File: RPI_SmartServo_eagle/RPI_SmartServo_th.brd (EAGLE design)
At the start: 75 x 60 mm, 39 parts, among them Q1 MCP9701A-E/TO, U1 ZXCT1009

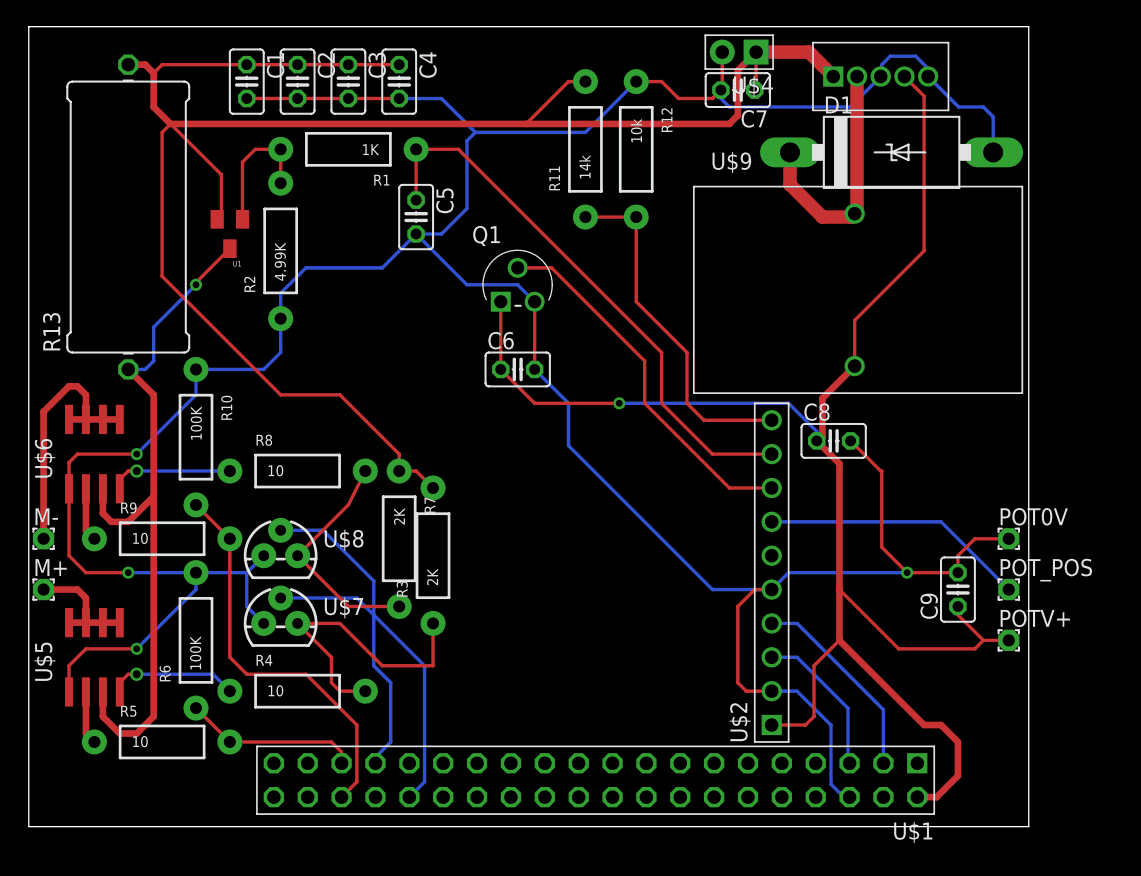
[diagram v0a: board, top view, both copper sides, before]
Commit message: Ground plane added 	modificado: RPI_SmartServo_eagle/RPI_SmartServo_th.brd
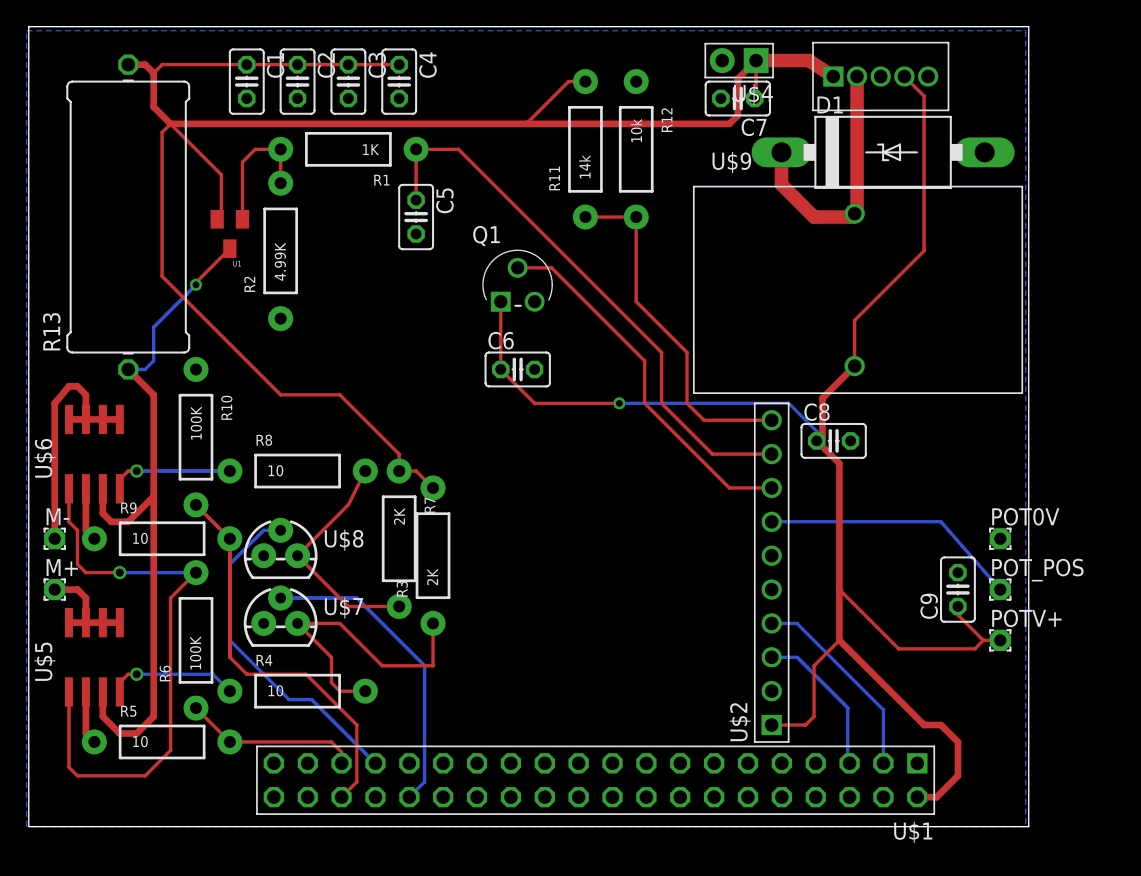
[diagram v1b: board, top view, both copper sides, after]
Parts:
- moved M+ 0.83 mm to (2.10, 17.8)
- moved M- 0.83 mm to (2.10, 21.6)
- moved D1 0.64 mm to (64.2, 50.6)
- moved C7 0.63 mm to (53.3, 54.6)
- moved U$4 0.63 mm to (54.7, 57.5)
- moved POT0V 0.63 mm to (73.0, 21.6)
- moved POTV+ 0.63 mm to (73.0, 14.0)
- moved POT_POS 0.63 mm to (73.0, 17.8)
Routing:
- net GND: track 257.3 -> 43.5 mm, vias 4 -> 1
- net EN_A: track 30.0 -> 42.5 mm
- net PWM_1: track 23.2 -> 25.3 mm
- net +12V: track 136.7 -> 135.7 mm
- net N$4: track 9.09 -> 8.26 mm
- net +5V: track 124.8 -> 124.2 mm
- net N$10: track 18.7 -> 19.4 mm
- added copper zone on layer 16, net GND

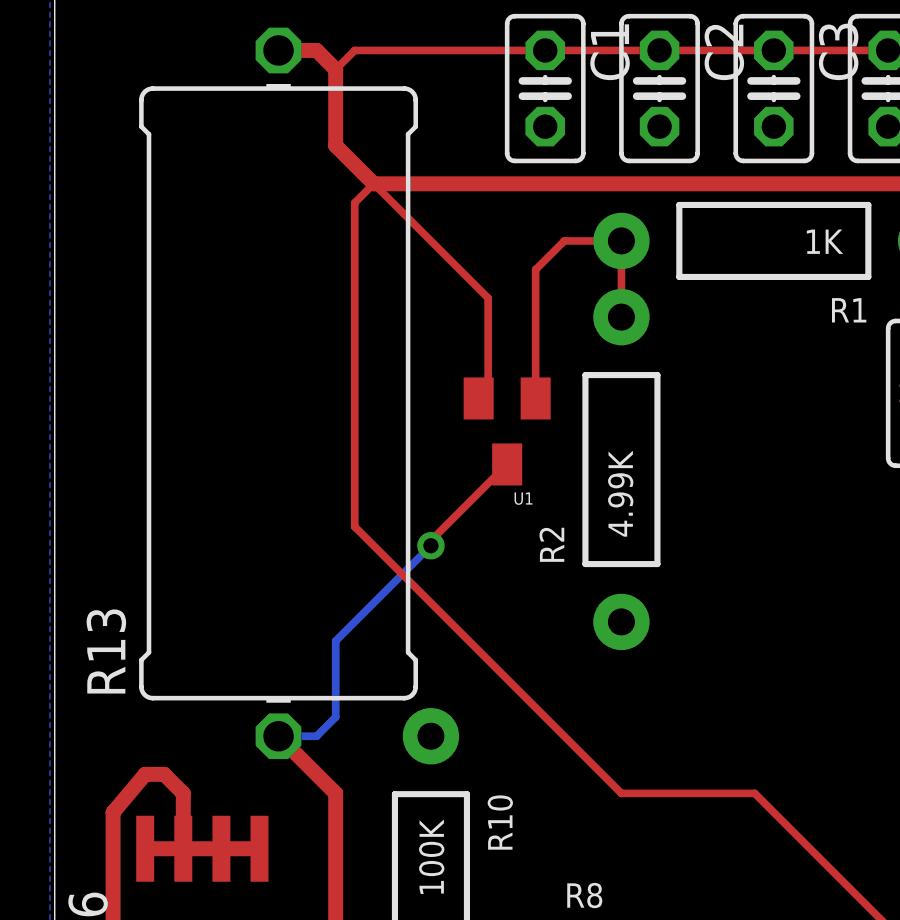
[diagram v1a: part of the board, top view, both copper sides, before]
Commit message: Changed the Current Sensor 	modificado: RPI_SmartServo_eagle/RPI_SmartServo_th.brd 	modificado: RPI_SmartServo_eagle/RPI_SmartServo_th.sch
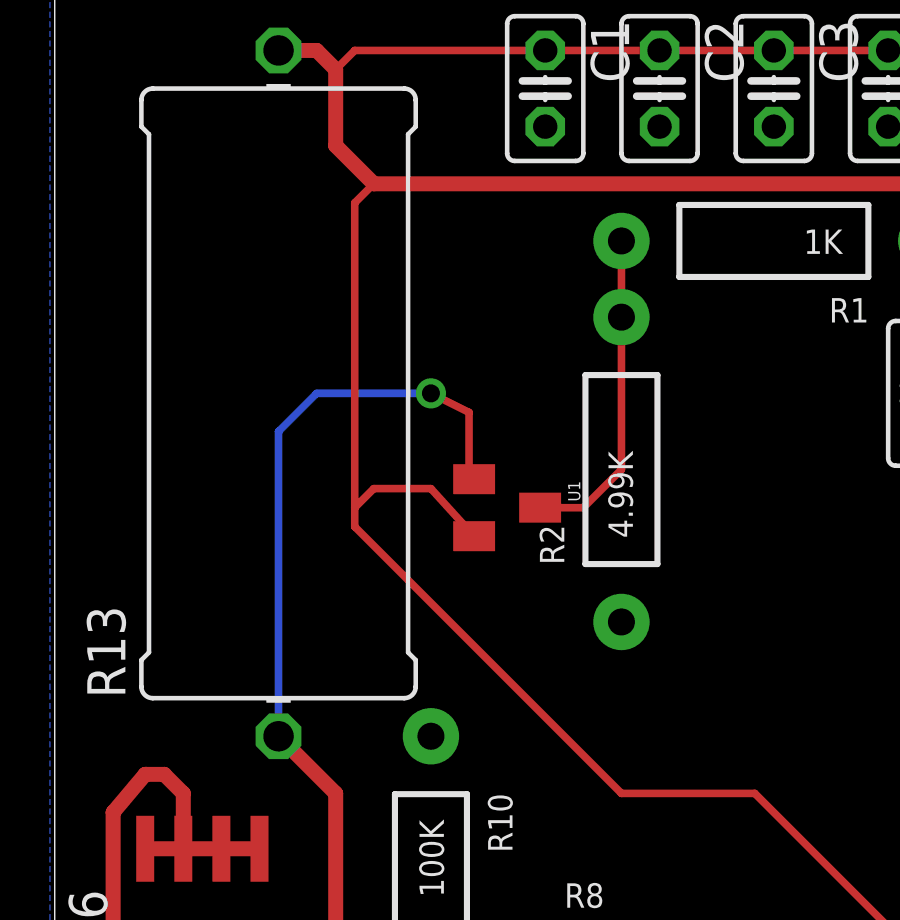
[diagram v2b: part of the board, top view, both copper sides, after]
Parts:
- U1: device WSNlib:SOT23 -> 00LibreriaErle:SOT23
- moved U1 2.54 mm to (15.2, 41.9), turned to 270 degrees
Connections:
- net N$1: now also U1.3; no longer U1.1
- net N$12: now also U1.1; no longer U1.3
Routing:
- net N$12: track 53.2 -> 59.7 mm
- net +12V: track 135.7 -> 131.7 mm
- net N$1: track 10.1 -> 10.9 mm
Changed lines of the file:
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@@
 <wire x1="75.16" y1="60" x2="0.16" y2="60" width="0" layer="20"/>
 <wire x1="0.16" y1="60" x2="0.16" y2="0" width="0" layer="20"/>
+<dimension x1="0" y1="0" x2="0.16" y2="60" x3="-10.239096875" y3="30.027515625" textsize="1.778" layer="1"/>
+<dimension x1="0" y1="0" x2="75.16" y2="0" x3="37.58" y3="-12.7" textsize="1.778" layer="1"/>
+<dimension x1="75" y1="0" x2="10" y2="0" x3="42.5" y3="-5.715" textsize="1.778" layer="1"/>
+<dimension x1="0" y1="0" x2="0" y2="30" x3="-5.08" y3="15" textsize="1.778" layer="1"/>
 </plain>
 <attributes>
@@
 <element name="U$8" library="00LibreriaErle" package="TO-92" value="2N7008G" x="19.05" y="20.32"/>
 <element name="U$9" library="00LibreriaErle" package="KM-4" value="PE-53113NL" x="50.038" y="48.006"/>
-<element name="U1" library="WSNlib" package="SOT23" value="ZXCT1009" x="15.24" y="44.45" rot="R180"/>
 <element name="Q1" library="00LibreriaErle" package="TO127P254X533-3" value="MCP9701A-E/TO" x="38.1" y="41.91">
 <attribute name="SUPPLIER" value="Microchip" x="38.1" y="41.91" size="1.778" layer="27" display="off"/>
@@
 <element name="M+" library="wirepad" package="1,6/0,9" value="" x="2.105" y="17.78"/>
 <element name="M-" library="wirepad" package="1,6/0,9" value="" x="2.105" y="21.59"/>
+<element name="U1" library="00LibreriaErle" package="SOT23" value="ZXCT1009" x="15.24" y="41.91" rot="R270"/>
 </elements>
 <signals>
@@
 <signal name="N$1">
 <contactref element="R1" pad="P$2"/>
-<contactref element="U1" pad="1"/>
 <contactref element="R2" pad="P$2"/>
 <wire x1="19.05" y1="48.26" x2="19.05" y2="50.8" width="0.254" layer="1"/>
-<wire x1="19.05" y1="50.8" x2="17.145" y2="50.8" width="0.254" layer="1"/>
-<wire x1="17.145" y1="50.8" x2="16.19" y2="49.845" width="0.254" layer="1"/>
-<wire x1="16.19" y1="49.845" x2="16.19" y2="45.55" width="0.254" layer="1"/>
+<contactref element="U1" pad="3"/>
+<wire x1="16.34" y1="41.91" x2="17.78" y2="41.91" width="0.254" layer="1"/>
+<wire x1="17.78" y1="41.91" x2="19.05" y2="43.18" width="0.254" layer="1"/>
+<wire x1="19.05" y1="43.18" x2="19.05" y2="48.26" width="0.254" layer="1"/>
 </signal>
 <signal name="CURRENT">
@@
 </signal>
 <signal name="N$12">
-<contactref element="U1" pad="3"/>
 <contactref element="R13" pad="1"/>
 <contactref element="U$5" pad="3"/>
@@
 <wire x1="9.525" y1="8.255" x2="9.525" y2="24.765" width="0.5" layer="1"/>
 <wire x1="5.715" y1="23.495" x2="5.715" y2="25.34" width="0.5" layer="1"/>
-<wire x1="15.24" y1="43.35" x2="12.7" y2="40.81" width="0.254" layer="1"/>
-<wire x1="12.7" y1="40.81" x2="12.7" y2="40.64" width="0.254" layer="1"/>
-<via x="12.7" y="40.64" extent="1-16" drill="0.508" shape="square"/>
-<wire x1="12.7" y1="40.64" x2="9.525" y2="37.465" width="0.254" layer="16"/>
-<wire x1="9.525" y1="37.465" x2="9.525" y2="34.925" width="0.254" layer="16"/>
-<wire x1="9.525" y1="34.925" x2="8.89" y2="34.29" width="0.254" layer="16"/>
-<wire x1="8.89" y1="34.29" x2="7.62" y2="34.29" width="0.254" layer="16"/>
+<contactref element="U1" pad="1"/>
+<wire x1="7.62" y1="34.29" x2="7.62" y2="44.45" width="0.254" layer="16"/>
+<wire x1="7.62" y1="44.45" x2="8.89" y2="45.72" width="0.254" layer="16"/>
+<wire x1="8.89" y1="45.72" x2="12.7" y2="45.72" width="0.254" layer="16"/>
+<via x="12.7" y="45.72" extent="1-16" drill="0.6" shape="square"/>
+<wire x1="12.7" y1="45.72" x2="13.97" y2="45.085" width="0.254" layer="1"/>
+<wire x1="13.97" y1="45.085" x2="13.97" y2="43.18" width="0.254" layer="1"/>
+<wire x1="13.97" y1="43.18" x2="14.14" y2="42.86" width="0.254" layer="1"/>
 </signal>
 <signal name="N$10">
@@
 <contactref element="U$3" pad="1"/>
 <contactref element="C7" pad="1"/>
-<contactref element="U1" pad="2"/>
 <contactref element="R13" pad="2"/>
 <contactref element="C4" pad="1"/>
@@
 <wire x1="24.13" y1="57.15" x2="27.94" y2="57.15" width="0.254" layer="1"/>
 <wire x1="10.795" y1="52.705" x2="10.16" y2="52.07" width="0.254" layer="1"/>
-<wire x1="10.16" y1="52.07" x2="10.16" y2="41.275" width="0.254" layer="1"/>
+<wire x1="10.16" y1="52.07" x2="10.16" y2="41.91" width="0.254" layer="1"/>
+<wire x1="10.16" y1="41.91" x2="10.16" y2="41.275" width="0.254" layer="1"/>
 <wire x1="10.16" y1="41.275" x2="19.05" y2="32.385" width="0.254" layer="1"/>
 <wire x1="19.05" y1="32.385" x2="23.495" y2="32.385" width="0.254" layer="1"/>
 <wire x1="23.495" y1="32.385" x2="27.94" y2="27.94" width="0.254" layer="1"/>
 <wire x1="27.94" y1="27.94" x2="27.94" y2="26.67" width="0.254" layer="1"/>
-<wire x1="14.29" y1="45.55" x2="14.605" y2="45.865" width="0.254" layer="1"/>
-<wire x1="14.605" y1="45.865" x2="14.605" y2="48.895" width="0.254" layer="1"/>
-<wire x1="14.605" y1="48.895" x2="10.795" y2="52.705" width="0.254" layer="1"/>
 <wire x1="41.91" y1="55.88" x2="40.64" y2="55.88" width="0.254" layer="1"/>
 <wire x1="40.64" y1="55.88" x2="37.465" y2="52.705" width="0.254" layer="1"/>
@@
 <wire x1="54.7116" y1="57.4548" x2="54.7116" y2="54.7116" width="0.254" layer="1"/>
 <wire x1="54.7116" y1="54.7116" x2="54.61" y2="54.61" width="0.254" layer="1"/>
+<contactref element="U1" pad="2"/>
+<wire x1="14.14" y1="40.96" x2="12.7" y2="42.545" width="0.254" layer="1"/>
+<wire x1="12.7" y1="42.545" x2="10.795" y2="42.545" width="0.254" layer="1"/>
+<wire x1="10.795" y1="42.545" x2="10.16" y2="41.91" width="0.254" layer="1"/>
 </signal>
 <signal name="+5V">
